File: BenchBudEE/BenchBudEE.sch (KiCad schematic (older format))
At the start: 0 parts

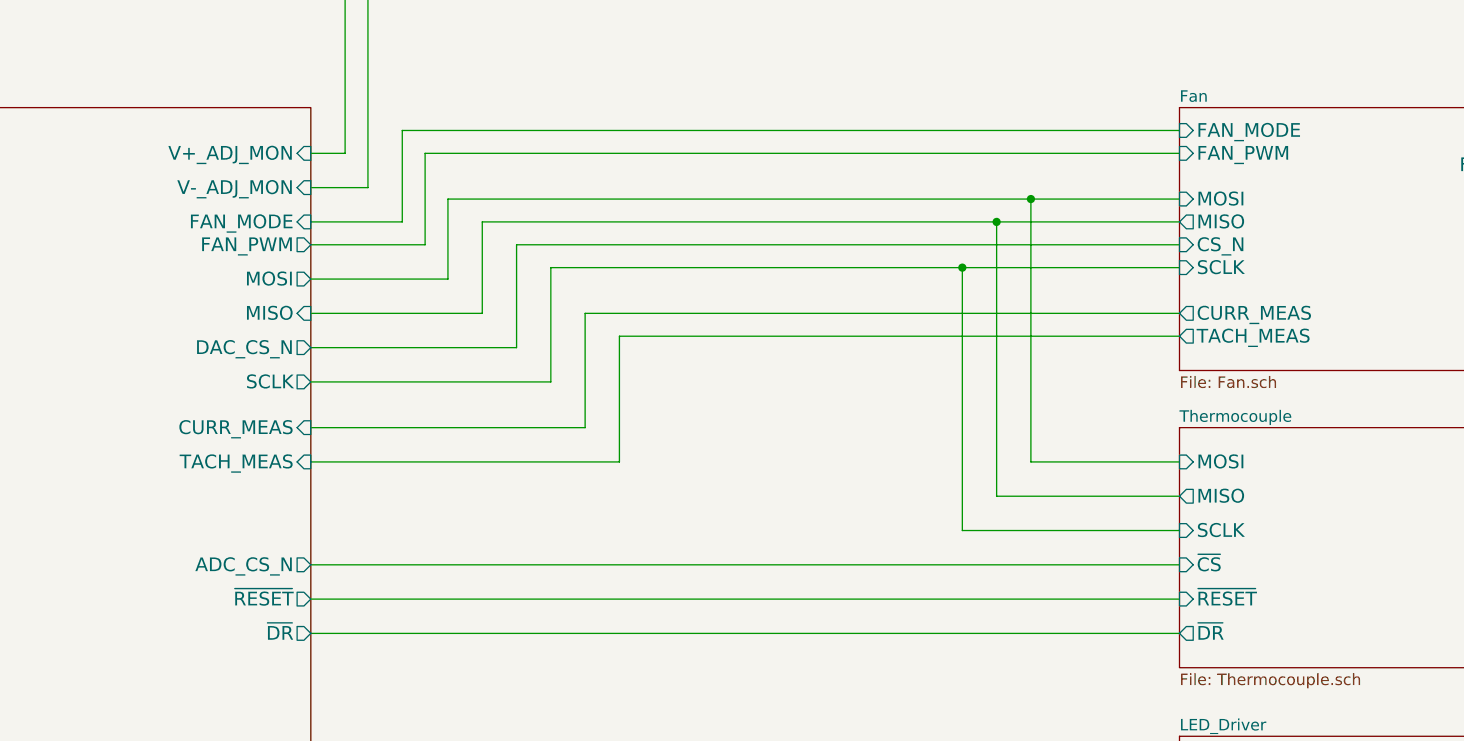
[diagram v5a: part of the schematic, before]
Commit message: Associating and Placing Fan Module
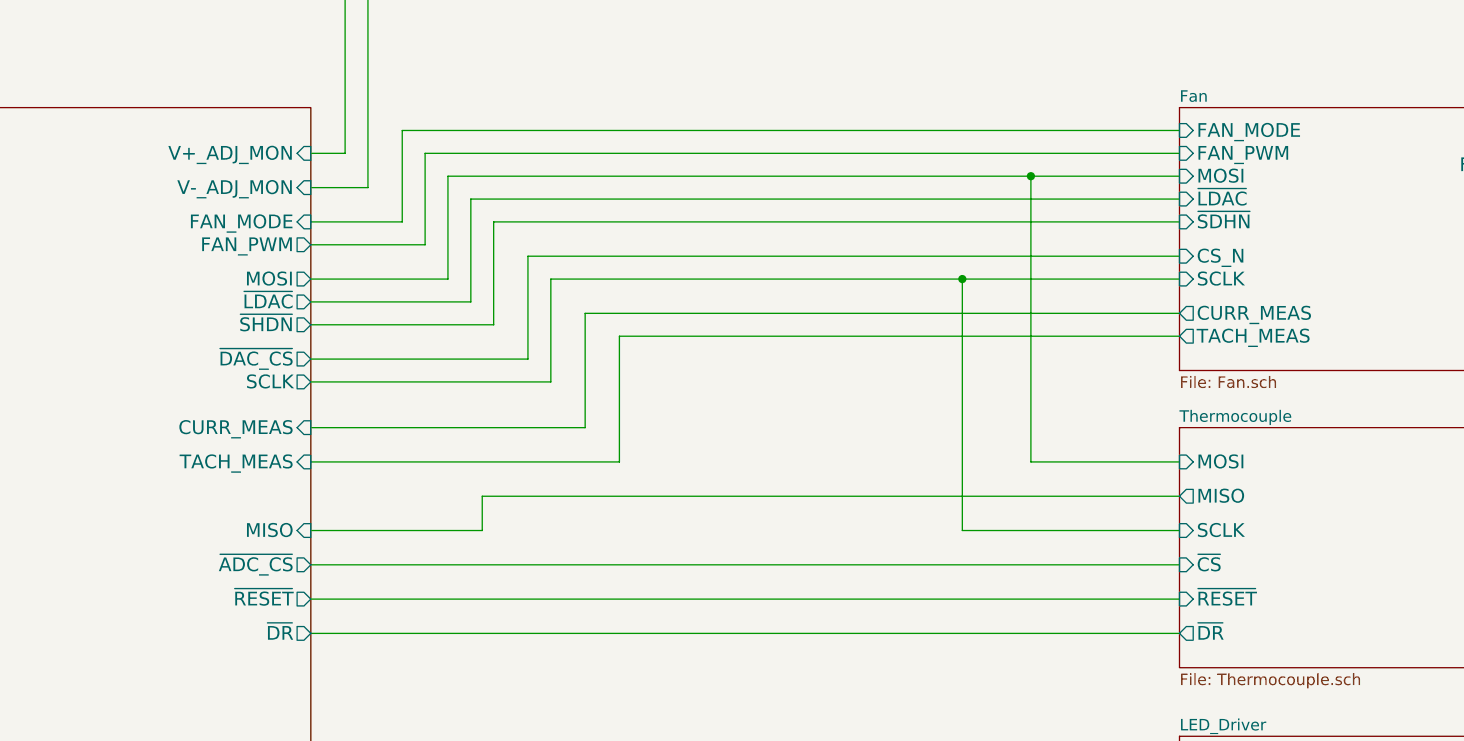
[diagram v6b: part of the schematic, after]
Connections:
- wire segments 54 -> 58
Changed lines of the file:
@@
 F1 "Arduino.sch" 39
 F2 "MOSI" O R 3300 3500 60
-F3 "MISO" I R 3300 3650 60
+F3 "MISO" I R 3300 4600 60
 F4 "SCLK" O R 3300 3950 60
 F5 "TACH_MEAS" I R 3300 4300 60
@@
 F10 "V-_ADJ_MON" I R 3300 3100 60
 F11 "LED_EN_PWM" O R 3300 5650 60
-F12 "DAC_CS_N" O R 3300 3800 60
-F13 "ADC_CS_N" O R 3300 4750 60
-F14 "FAN_PWM" O R 3300 3350 60
-F15 "FAN_MODE" I R 3300 3250 60
-F16 "~DR" O R 3300 5050 60
-F17 "~RESET" O R 3300 4900 60
+F12 "FAN_PWM" O R 3300 3350 60
+F13 "FAN_MODE" I R 3300 3250 60
+F14 "~DR" O R 3300 5050 60
+F15 "~RESET" O R 3300 4900 60
+F16 "~SHDN" O R 3300 3700 60
+F17 "~LDAC" O R 3300 3600 60
+F18 "~DAC_CS" O R 3300 3850 60
+F19 "~ADC_CS" O R 3300 4750 60
 $EndSheet
 Wire Wire Line
@@
 	3300 3500 3900 3500
 Wire Wire Line
-	3900 3500 3900 3150
+	3900 3500 3900 3050
 Wire Wire Line
-	3900 3150 7100 3150
+	3900 3050 7100 3050
 Wire Wire Line
-	4050 3250 7100 3250
+	4050 4600 3300 4600
 Wire Wire Line
-	4050 3650 3300 3650
+	3300 3850 4250 3850
 Wire Wire Line
-	3300 3800 4200 3800
+	4250 3850 4250 3400
 Wire Wire Line
-	4200 3800 4200 3350
-Wire Wire Line
-	4200 3350 7100 3350
+	4250 3400 7100 3400
 Wire Wire Line
 	3300 3950 4350 3950
 Wire Wire Line
-	4350 3450 7100 3450
+	4350 3500 7100 3500
 Wire Wire Line
 	3300 4150 4500 4150
@@
 	7100 4300 6450 4300
 Wire Wire Line
-	6450 4300 6450 3150
-Connection ~ 6450 3150
+	6450 4300 6450 3050
+Connection ~ 6450 3050
 Wire Wire Line
-	6300 4450 7100 4450
-Wire Wire Line
-	6300 4450 6300 3250
-Connection ~ 6300 3250
+	4050 4450 7100 4450
 Wire Wire Line
 	7100 4600 6150 4600
 Wire Wire Line
-	6150 4600 6150 3450
-Connection ~ 6150 3450
+	6150 4600 6150 3500
+Connection ~ 6150 3500
 Wire Wire Line
 	3300 4750 7100 4750
@@
 F0 "Fan" 50
 F1 "Fan.sch" 50
-F2 "MOSI" I L 7100 3150 60
-F3 "MISO" O L 7100 3250 60
-F4 "CS_N" I L 7100 3350 60
-F5 "SCLK" I L 7100 3450 60
-F6 "FAN_OUT+" O R 8850 3000 60
-F7 "TACH_IN" I R 8850 3600 60
-F8 "TACH_MEAS" O L 7100 3750 60
-F9 "CURR_MEAS" O L 7100 3650 60
-F10 "FAN_OUT-" O R 8850 3150 60
-F11 "FAN_PWM" I L 7100 2950 60
-F12 "FAN_MODE" I L 7100 2850 60
+F2 "MOSI" I L 7100 3050 60
+F3 "CS_N" I L 7100 3400 60
+F4 "SCLK" I L 7100 3500 60
+F5 "FAN_OUT+" O R 8850 3000 60
+F6 "TACH_IN" I R 8850 3600 60
+F7 "TACH_MEAS" O L 7100 3750 60
+F8 "CURR_MEAS" O L 7100 3650 60
+F9 "FAN_OUT-" O R 8850 3150 60
+F10 "FAN_PWM" I L 7100 2950 60
+F11 "FAN_MODE" I L 7100 2850 60
+F12 "~LDAC" I L 7100 3150 60
+F13 "~SDHN" I L 7100 3250 60
 $EndSheet
 Wire Wire Line
-	4050 3250 4050 3650
-Wire Wire Line
-	4350 3950 4350 3450
+	4350 3950 4350 3500
 Wire Wire Line
 	3700 2850 7100 2850
@@
 Wire Wire Line
 	3300 5050 7100 5050
+Wire Wire Line
+	4050 4450 4050 4600
+Wire Wire Line
+	7100 3150 4000 3150
+Wire Wire Line
+	4000 3150 4000 3600
+Wire Wire Line
+	4000 3600 3300 3600
+Wire Wire Line
+	3300 3700 4100 3700
+Wire Wire Line
+	4100 3700 4100 3250
+Wire Wire Line
+	4100 3250 7100 3250
 $EndSCHEMATC
